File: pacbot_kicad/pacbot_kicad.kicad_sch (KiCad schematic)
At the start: 14 parts, among them M3 Motor_DC, M4 Motor_DC, U1 Teensy4.1, U11 BD65496MUV, U12 BD65496MUV, U13 BD65496MUV, U14 BD65496MUV, U2 TCA9548A, U21 VL6180X, U22 VL6180X, U23 VL6180X, U24 VL6180X

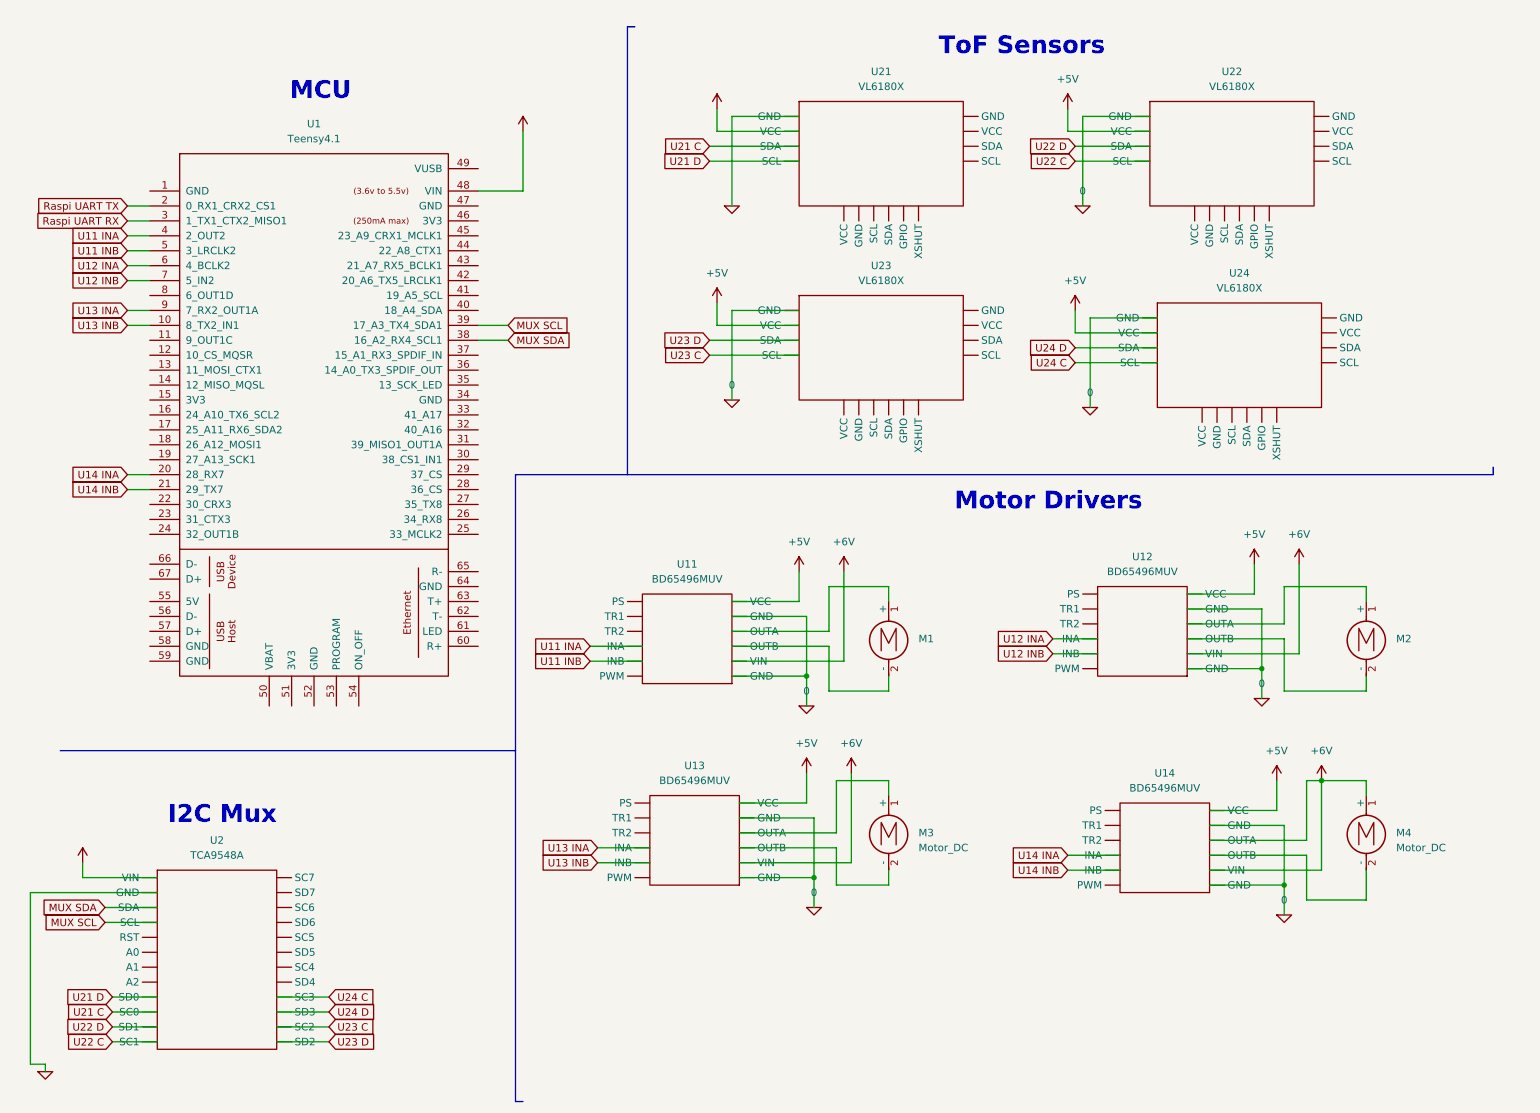
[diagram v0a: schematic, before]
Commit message: electronics: add encoder symbol, redo schematic
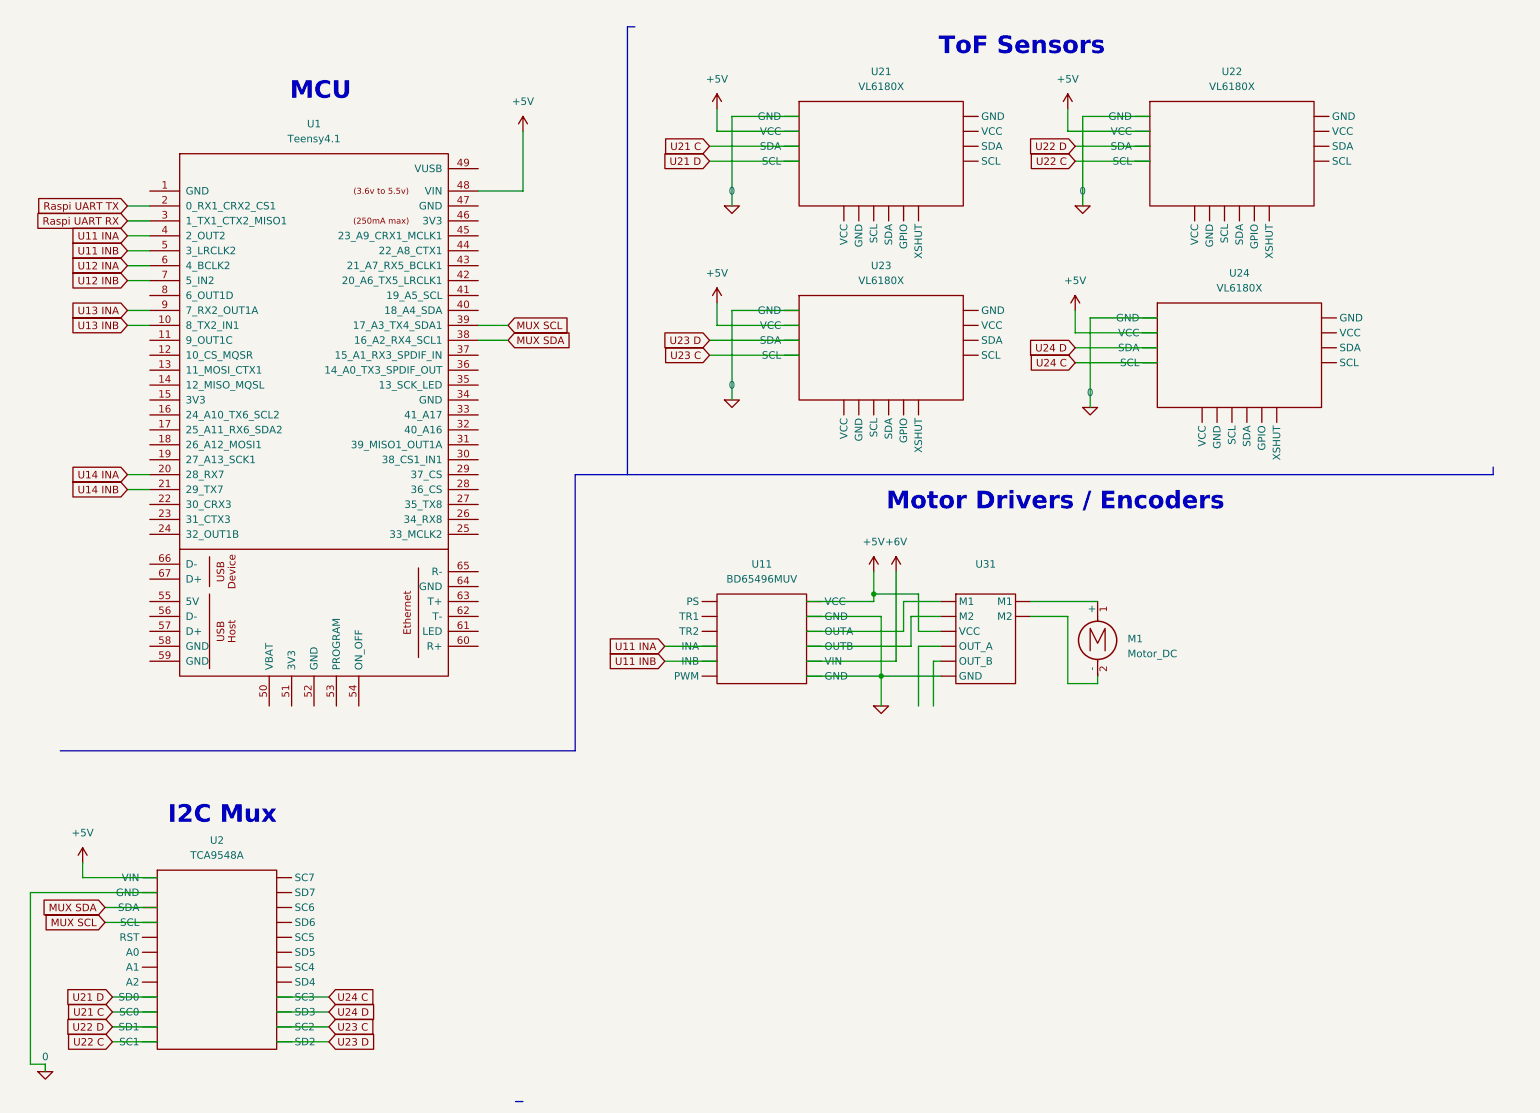
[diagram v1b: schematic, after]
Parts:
- removed M2: (no value), symbol Motor:Motor_DC
- removed M3, M4: Motor_DC, symbol Motor:Motor_DC
- removed U12, U13, U14: BD65496MUV, symbol Pololu:BD65496MUV
- added U31: (no value), symbol Pololu:4760_Magnetic_Encoder
- M1: value (none) -> Motor_DC
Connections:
- net +5V: now also U31. (VCC)
- net 0: now also U31. (VCC)
- net at M1.1 (+): now also U31. (VCC); no longer U11. (VIN)
- net at M1.2 (-): now also U31. (VCC); no longer U11. (VIN)
- new net: U11. (VIN), U31. (VCC) (x2)
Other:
- note added: "Motor Drivers / Encoders"
- note removed: "Motor Drivers"
- moved on the sheet: M1, U11

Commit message: electronics: updated symbols, finished adding encoders
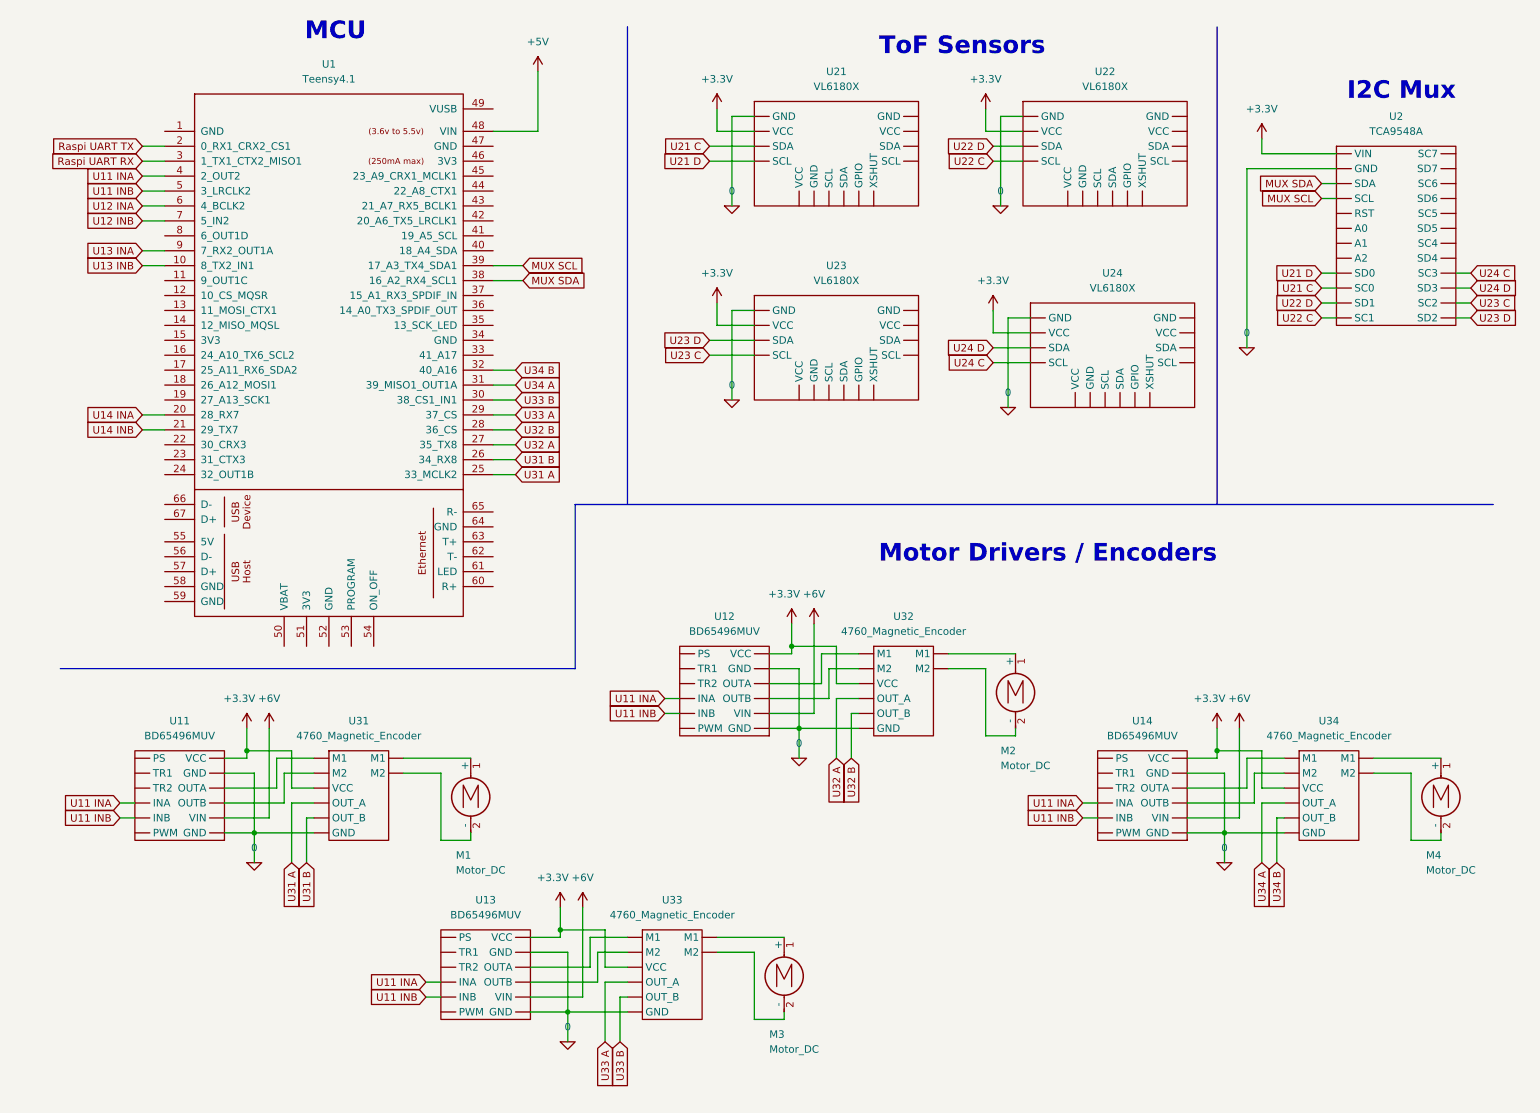
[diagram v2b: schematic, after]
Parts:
- added M2, M3, M4: Motor_DC, symbol Motor:Motor_DC
- added U12, U13, U14: BD65496MUV, symbol Pololu:BD65496MUV
- added U32, U33, U34: 4760_Magnetic_Encoder, symbol Pololu:4760_Magnetic_Encoder
- U31: value (none) -> 4760_Magnetic_Encoder
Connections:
- net +5V: no longer U11. (VIN), U2. (VIN), U21. (XSHUT), U22. (XSHUT), U23. (XSHUT), U24. (XSHUT), U31. (VCC)
- net +6V: now also U12. (VIN), U13. (VIN), U14. (VIN)
- net 0: now also U12. (VIN), U13. (VIN), U14. (VIN), U32. (VCC), U33. (VCC), U34. (VCC)
- net U11 INA: now also U12. (VIN), U13. (VIN), U14. (VIN)
- net U11 INB: now also U12. (VIN), U13. (VIN), U14. (VIN)
- net U31 B: now reaches U31. (VCC)
- net U31 B: now also U1.26 (34_RX8)
- net U31 A: now reaches U1.25 (33_MCLK2)
- net U31 A: now also U31. (VCC)
- net U32 A: now reaches U1.27 (35_TX8)
- net U32 A: now also U32. (VCC)
- net U32 B: now reaches U1.28 (36_CS)
- net U32 B: now also U32. (VCC)
- net U33 A: now reaches U1.29 (37_CS)
- net U33 A: now also U33. (VCC)
- net U33 B: now reaches U1.30 (38_CS1_IN1)
- net U33 B: now also U33. (VCC)
- net U34 A: now reaches U1.31 (39_MISO1_OUT1A)
- net U34 A: now also U34. (VCC)
- net U34 B: now reaches U1.32 (40_A16)
- net U34 B: now also U34. (VCC)
- new net: M3.1 (+), U33. (VCC)
- new net: M3.2 (-), U33. (VCC)
- new net: M4.1 (+), U34. (VCC)
- new net: M4.2 (-), U34. (VCC)
- new net: U14. (VIN), U34. (VCC) (x2)
- new net: U11. (VIN), U31. (VCC) (x2)
- new net: U12. (VIN), U32. (VCC) (x2)
- new net: M2.1 (+), U32. (VCC)
- new net: M2.2 (-), U32. (VCC)
- new net: U13. (VIN), U33. (VCC) (x2)
- new net +3V3: U11. (VIN), U12. (VIN), U13. (VIN), U14. (VIN), U2. (VIN), U21. (XSHUT), U22. (XSHUT), U23. (XSHUT), U24. (XSHUT), U31. (VCC), U32. (VCC), U33. (VCC), U34. (VCC)
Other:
- moved on the sheet: M1, U1, U11, U2, U21, U22, U23, U24, U31

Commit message: electronics: kicad fix error at U21
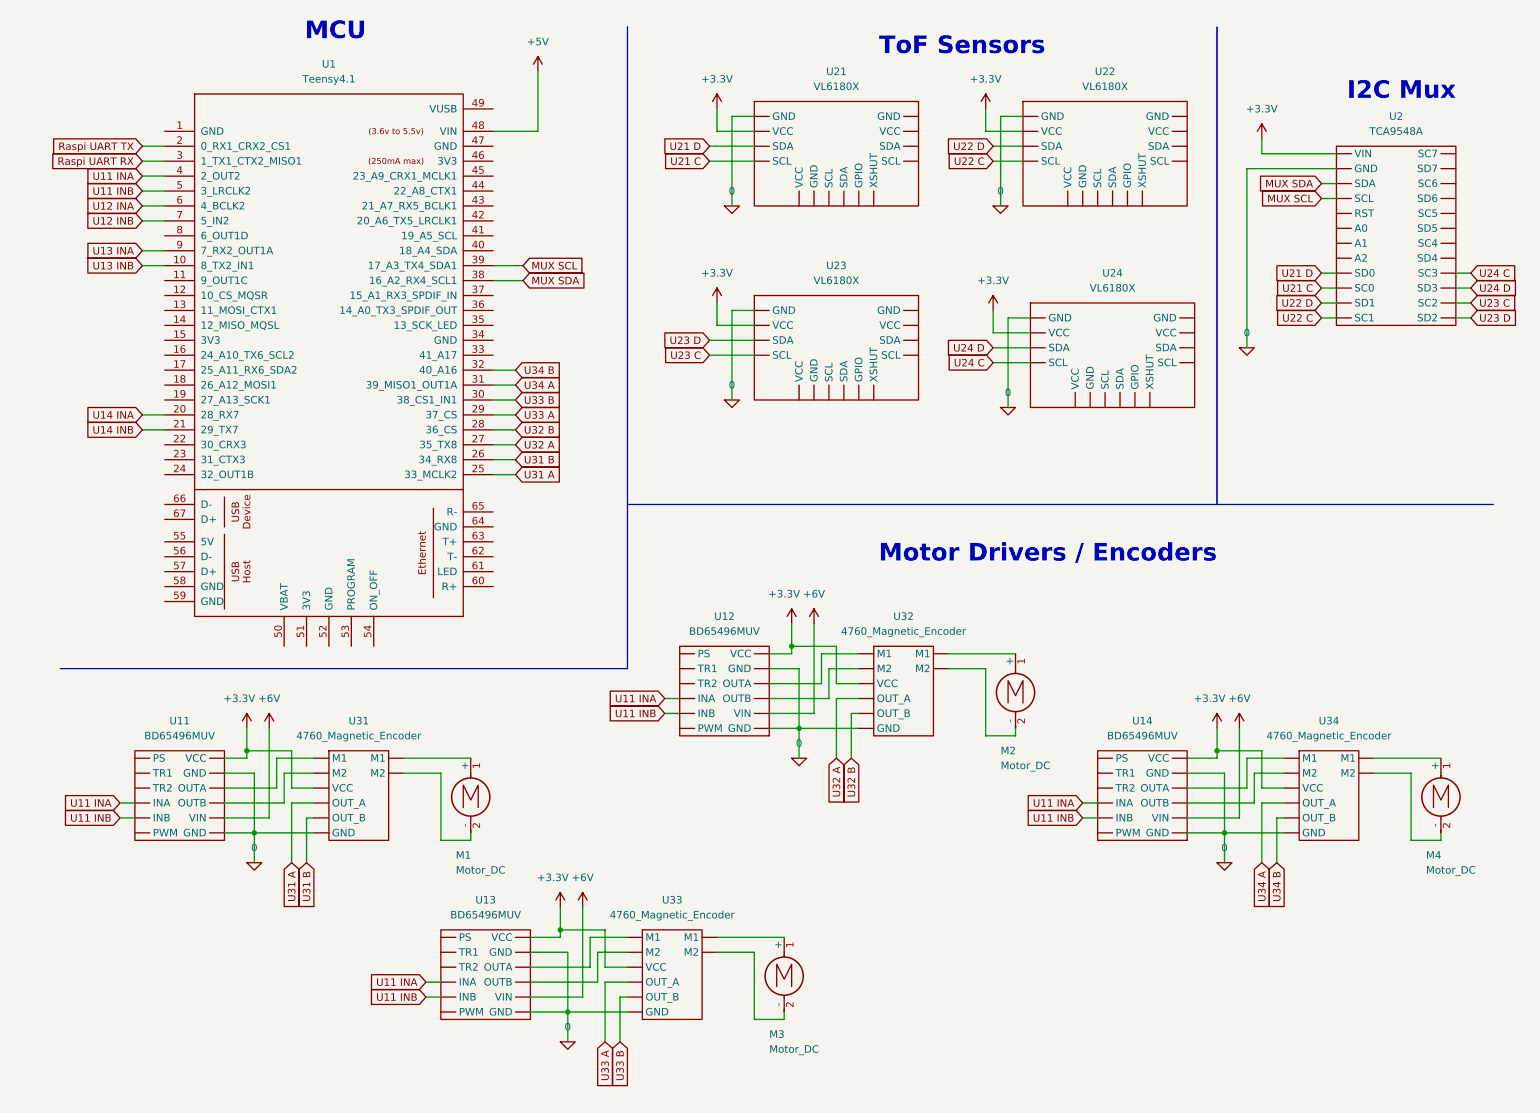
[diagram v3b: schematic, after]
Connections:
- new net: U14. (VIN), U34. (VCC) (x2)
- new net: U11. (VIN), U31. (VCC) (x2)
- new net: U12. (VIN), U32. (VCC) (x2)
- new net: U13. (VIN), U33. (VCC) (x2)

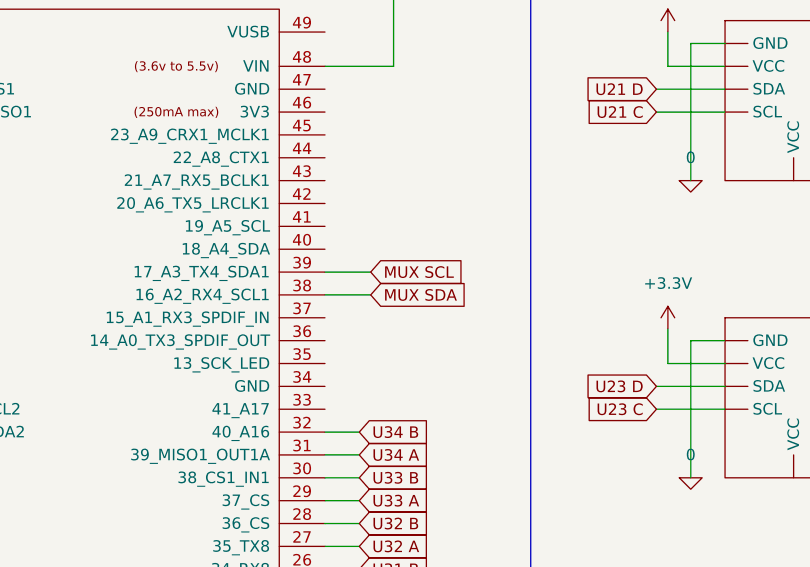
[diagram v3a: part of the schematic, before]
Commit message: electronics: fixed error on teensy I2C pin
thanks dylan!
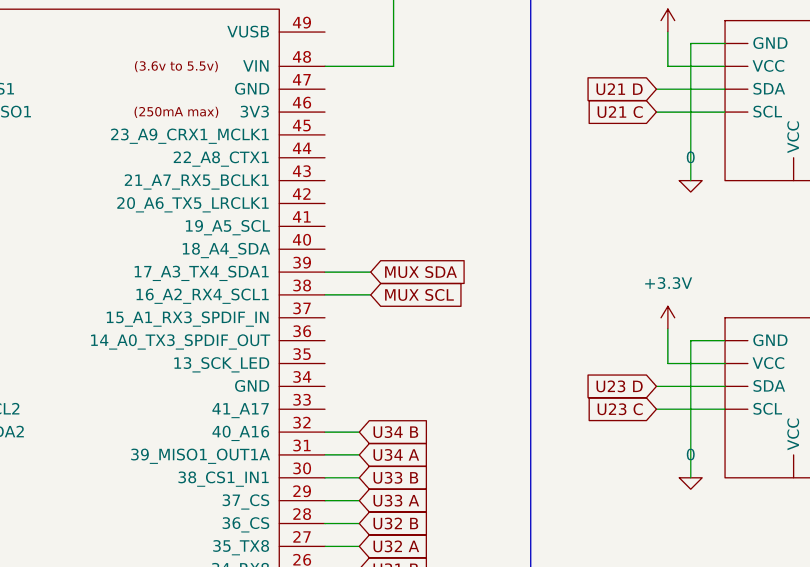
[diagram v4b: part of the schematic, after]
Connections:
- net MUX SCL: now also U1.38 (16_A2_RX4_SCL1); no longer U1.39 (17_A3_TX4_SDA1)
- net MUX SDA: now also U1.39 (17_A3_TX4_SDA1); no longer U1.38 (16_A2_RX4_SCL1)
- new net: U14. (VIN), U34. (VCC) (x2)
- new net: U11. (VIN), U31. (VCC) (x2)
- new net: U12. (VIN), U32. (VCC) (x2)
- new net: U13. (VIN), U33. (VCC) (x2)
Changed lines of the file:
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@@
     (stroke (width 0) (type default) (color 0 0 0 1))
-  )
-  (wire (pts (xy 96.52 57.15) (xy 91.44 57.15))
-    (stroke (width 0) (type default) (color 0 0 0 0))
   )
   (wire (pts (xy 219.71 40.64) (xy 219.71 71.12))
@@
     (stroke (width 0) (type default) (color 0 0 0 1))
   )
+  (wire (pts (xy 91.44 59.69) (xy 96.52 59.69))
+    (stroke (width 0) (type default) (color 0 0 0 0))
+  )
   (wire (pts (xy 182.88 66.04) (xy 179.07 66.04))
     (stroke (width 0) (type default) (color 0 0 0 1))
@@
     (stroke (width 0) (type default) (color 0 0 0 0))
   )
-  (wire (pts (xy 96.52 59.69) (xy 91.44 59.69))
-    (stroke (width 0) (type default) (color 0 0 0 0))
-  )
   (wire (pts (xy 91.44 90.17) (xy 95.25 90.17))
     (stroke (width 0) (type default) (color 0 0 0 0))
@@
   )
   (wire (pts (xy 120.65 133.35) (xy 123.19 133.35))
+    (stroke (width 0) (type default) (color 0 0 0 0))
+  )
+  (wire (pts (xy 91.44 57.15) (xy 96.52 57.15))
     (stroke (width 0) (type default) (color 0 0 0 0))
   )
@@
     )
   )
-  (global_label "MUX SCL" (shape input) (at 96.52 57.15 0) (fields_autoplaced)
-    (effects (font (size 1.27 1.27)) (justify left))
-    (property "Intersheet References" "${INTERSHEET_REFS}" (id 0) (at 107.3998 57.0706 0)
-      (effects (font (size 1.27 1.27)) (justify left) hide)
-    )
-  )
-  (global_label "MUX SDA" (shape input) (at 96.52 59.69 0) (fields_autoplaced)
-    (effects (font (size 1.27 1.27)) (justify left))
-    (property "Intersheet References" "${INTERSHEET_REFS}" (id 0) (at 107.4602 59.6106 0)
-      (effects (font (size 1.27 1.27)) (justify left) hide)
-    )
+  (global_label "MUX SCL" (shape input) (at 96.52 59.69 0) (fields_autoplaced)
+    (effects (font (size 1.27 1.27)) (justify left))
+    (property "Intersheet References" "${INTERSHEET_REFS}" (id 0) (at 107.3998 59.6106 0)
+      (effects (font (size 1.27 1.27)) (justify left) hide)
+    )
+  )
+  (global_label "MUX SDA" (shape input) (at 96.52 57.15 0) (fields_autoplaced)
+    (effects (font (size 1.27 1.27)) (justify left))
+    (property "Intersheet References" "${INTERSHEET_REFS}" (id 0) (at 107.4602 57.0706 0)
+      (effects (font (size 1.27 1.27)) (justify left) hide)
+    )
